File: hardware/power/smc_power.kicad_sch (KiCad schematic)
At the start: 98 parts, among them IC1 LM393DR2GH, J1 Screw_Terminal_01x02, J2 48V Input, J3 48V Output, J4 24V Brake Output, J5 Logic Output, Q1 P40B10SL, U1 TPS54360DDA, U2 AP2112K-3.3, U3 TPS54360DDA, U4 TPS16630PWPR, U5 MCP1416, U6 TL431B_C54830630, U7 L78L12_SOT89

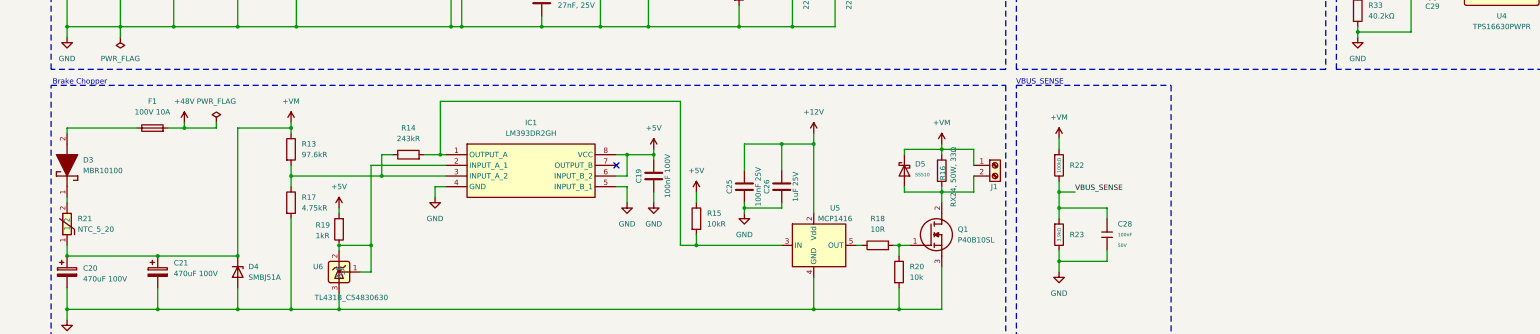
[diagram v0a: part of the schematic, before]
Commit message: hw(power): 48V input DM pi-filter (L4 2.2uH ETQP4M2R2KVK, C34/C35 2.2uF 100V X7R), closes #65
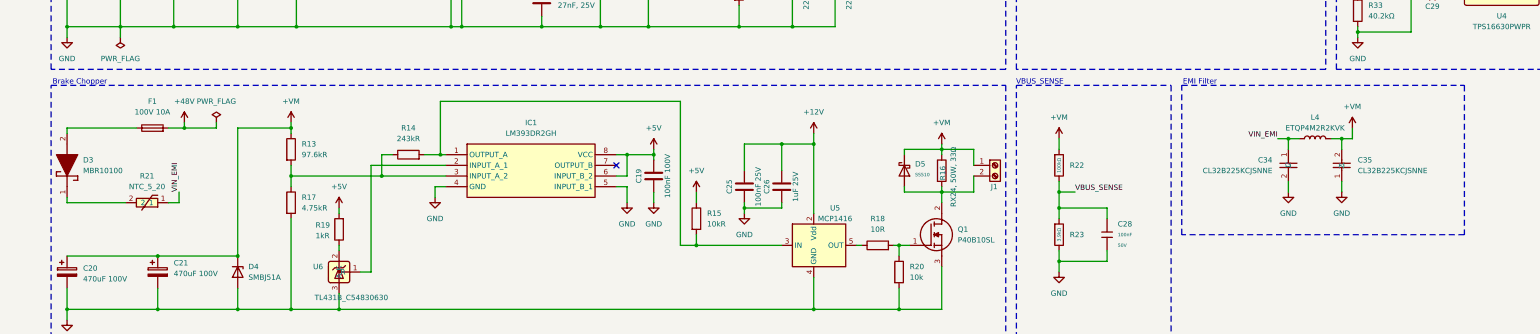
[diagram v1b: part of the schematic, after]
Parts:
- added C34, C35: CL32B225KCJSNNE, Capacitor_SMD:C_1210_3225Metric, symbol JLCImport:CL32B225KCJSNNE
- added L4: ETQP4M2R2KVK, Inductor_SMD:L_Panasonic_PCC-M0850M, symbol Device:L
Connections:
- net +VM: now also C35.2, L4.2; no longer R21.1
- net GND: now also C34.2, C35.1
- net at R19.1, U6.2 (K): no longer IC1.2 (INPUT_A_1), U6.1 (R)
- new net: IC1.2 (INPUT_A_1), U6.1 (R)
- new net VIN_EMI: C34.1, L4.1, R21.1
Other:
- note added: "EMI Filter"
- moved on the sheet: R21

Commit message: hw(power): +VM symbol from project lib, L4 LCSC field, refs #48
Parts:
- L4: LCSC (none) -> C230663
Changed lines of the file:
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@@
 			)
 		)
-		(property "Description" "C230663"
+		(property "LCSC" "C230663"
 			(at 318.77 227.33 0)
 			(hide yes)
@@
 	)
 	(symbol
-		(lib_id "power:+VM")
+		(lib_id "Step Motor Controller:+VM")
 		(at 327.66 224.79 0)
 		(unit 1)

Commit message: hw(power): final review fixes — TL431 REF-K via 0R, eFuse ILIM, notes; JLC resistors to project lib, refs #67
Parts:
- removed R30: 5.1kΩ, Resistor_SMD:R_0805_2012Metric_Pad1.20x1.40mm_HandSolder, symbol Step Motor Controller:R_0805_5p1k
- added R30: 12kΩ, Resistor_SMD:R_0805_2012Metric_Pad1.20x1.40mm_HandSolder, symbol Step Motor Controller:R_0805_12k
- added R36: 0Ω, Resistor_SMD:R_0805_2012Metric_Pad1.20x1.40mm_HandSolder, symbol Step Motor Controller:R_0805_0
- L4: LCSC C230663 -> (none)
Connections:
- net GND: now also R30.2
- net at R19.1, U6.2 (K): now also R36.1
- net at IC1.2 (INPUT_A_1), U6.1 (R): now also R36.2
- net at U4.11 (ILIM): now also R30.1
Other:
- note added: "!!PSU max ≤ 52 V"

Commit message: hw(power): re-apply +VM project-lib symbol and L4 LCSC field (lost on save), refs #67
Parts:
- L4: LCSC (none) -> C230663
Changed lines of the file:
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@@
 			)
 		)
-		(property "Description" "C230663"
+		(property "LCSC" "C230663"
 			(at 318.77 227.33 0)
 			(hide yes)
@@
 	)
 	(symbol
-		(lib_id "power:+VM")
+		(lib_id "Step Motor Controller:+VM")
 		(at 327.66 224.79 0)
 		(unit 1)

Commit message: hw(power): 4-layer 2oz/1oz stackup, PCB synced from schematic, refs #39
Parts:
- L4: LCSC C230663 -> (none)
- R16: footprint Resistor_THT:R_Axial_DIN0516_L15.5mm_D5.0mm_P25.40mm_Horizontal -> (none)
- R30: symbol Step Motor Controller:R_0805_12k -> PCM_JLCPCB-Resistors:0805,12kΩ
- R36: symbol Step Motor Controller:R_0805_0 -> PCM_JLCPCB-Resistors:0805,0Ω
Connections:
- net CHOP_DRAIN: now reaches D5.2, J1.2 (Pin_2), Q1.2 (D), R16.2
- net VIN_FUSED: now reaches D3.2 (A), F1.1
- net VIN_PROT: now reaches D3.1 (K), R21.2
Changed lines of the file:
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@@
 		)
 	)
+	(label "VIN_FUSED"
+		(at 21.59 224.79 0)
+		(effects
+			(font
+				(size 1.27 1.27)
+			)
+			(justify left bottom)
+		)
+	)
 	(label "TPS16630_FLT#"
 		(at 377.19 182.88 0)
@@
 		)
 	)
+	(label "VIN_PROT"
+		(at 24.13 242.57 0)
+		(effects
+			(font
+				(size 1.27 1.27)
+			)
+			(justify left bottom)
+		)
+	)
 	(label "SW_5V"
 		(at 127 172.72 0)
@@
 		)
 	)
+	(label "CHOP_DRAIN"
+		(at 237.49 236.22 270)
+		(effects
+			(font
+				(size 1.27 1.27)
+			)
+			(justify right bottom)
+		)
+	)
 	(label "VBUS_SENSE"
 		(at 100.33 27.94 0)
@@
 			)
 		)
-		(property "Footprint" "Resistor_THT:R_Axial_DIN0516_L15.5mm_D5.0mm_P25.40mm_Horizontal"
+		(property "Footprint" ""
 			(at 228.092 234.95 90)
 			(hide yes)
@@
 			)
 		)
-		(property "LCSC" "C230663"
+		(property "Description" "C230663"
 			(at 318.77 227.33 0)
 			(hide yes)
@@
 	)
 	(symbol
-		(lib_id "Step Motor Controller:+VM")
+		(lib_id "power:+VM")
 		(at 327.66 224.79 0)
 		(unit 1)
@@
 	)
 	(symbol
-		(lib_id "Step Motor Controller:R_0805_0")
+		(lib_id "PCM_JLCPCB-Resistors:0805,0Ω")
 		(at 90.17 254 90)
 		(unit 1)
@@
 	)
 	(symbol
-		(lib_id "Step Motor Controller:R_0805_12k")
+		(lib_id "PCM_JLCPCB-Resistors:0805,12kΩ")
 		(at 381 193.04 90)
 		(unit 1)

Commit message: hw(power): re-apply project-lib fixes overwritten by KiCad save (+VM, R30/R36, L4 LCSC), refs #39
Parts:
- L4: LCSC (none) -> C230663
- R30: symbol PCM_JLCPCB-Resistors:0805,12kΩ -> Step Motor Controller:R_0805_12k
- R36: symbol PCM_JLCPCB-Resistors:0805,0Ω -> Step Motor Controller:R_0805_0
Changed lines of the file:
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@@
 			)
 		)
-		(property "Description" "C230663"
+		(property "LCSC" "C230663"
 			(at 318.77 227.33 0)
 			(hide yes)
@@
 	)
 	(symbol
-		(lib_id "power:+VM")
+		(lib_id "Step Motor Controller:+VM")
 		(at 327.66 224.79 0)
 		(unit 1)
@@
 	)
 	(symbol
-		(lib_id "PCM_JLCPCB-Resistors:0805,0Ω")
+		(lib_id "Step Motor Controller:R_0805_0")
 		(at 90.17 254 90)
 		(unit 1)
@@
 	)
 	(symbol
-		(lib_id "PCM_JLCPCB-Resistors:0805,12kΩ")
+		(lib_id "Step Motor Controller:R_0805_12k")
 		(at 381 193.04 90)
 		(unit 1)
